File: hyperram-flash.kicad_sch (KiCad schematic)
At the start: 7 parts, among them U1 IS66WVH16M8DBLL-100B1LI

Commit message: Finish creating hierarchical buses and structure, start reconnecting signals
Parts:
- added C5: C_100n_0402, sodimm-ddr5-tester-footprints:C_0402_1005Metric, symbol sodimm-ddr5-tester:C_100n_0402
- added R10: R_100R_0402, sodimm-ddr5-tester-footprints:R_0402_1005Metric, symbol sodimm-ddr5-tester:R_100R_0402
- added R3: R_2k2_0402, sodimm-ddr5-tester-footprints:R_0402_1005Metric, symbol sodimm-ddr5-tester:R_2k2_0402
- added R4, R5: R_4k7_0402, sodimm-ddr5-tester-footprints:R_0402_1005Metric, symbol sodimm-ddr5-tester:R_4k7_0402
- added R6, R7, R8, R9: R_22R_0402, sodimm-ddr5-tester-footprints:R_0402_1005Metric, symbol sodimm-ddr5-tester:R_22R_0402
- added U3: S25FL128SAGNFI000, sodimm-ddr5-tester-footprints:WSON-8_6x8x0.5mm_P1.27mm, symbol sodimm-ddr5-tester:S25FL128SAGNFI000
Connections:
- net +3V3: now also C5.1, R3.1, R4.1, R5.1, U3.8 (V_{CC})
- net GND: now also C5.2, R10.2, U3.4 (V_{SS})
- new net: R7.1, U3.2 (SO/IO1)
- new net: R5.2, R8.1, U3.3 (~{WP}/IO2)
- new net: R4.2, R9.1, U3.7 (~{HOLD}/IO3)
- new net: R6.1, U3.5 (SI/IO0)
- new net FLASH.IO0: R6.2
- new net FLASH.IO1: R7.2
- new net FLASH.IO2: R8.2
- new net FLASH.IO3: R9.2
- new net FLASH.SCK: R10.1, U3.6 (SCK)
- new net FLASH.~{CS}: R3.2, U3.1 (~{CS})
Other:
- note added: "(Q)SPI flash"
- note added: "Master SPI Quad (x4) configuration scheme Follows Figure 2-14 7 Series FPGAs Configuration User Guide UG470 (v1.13.1)"
- moved on the sheet: C1, C2, C3, C4, R1, R2, U1

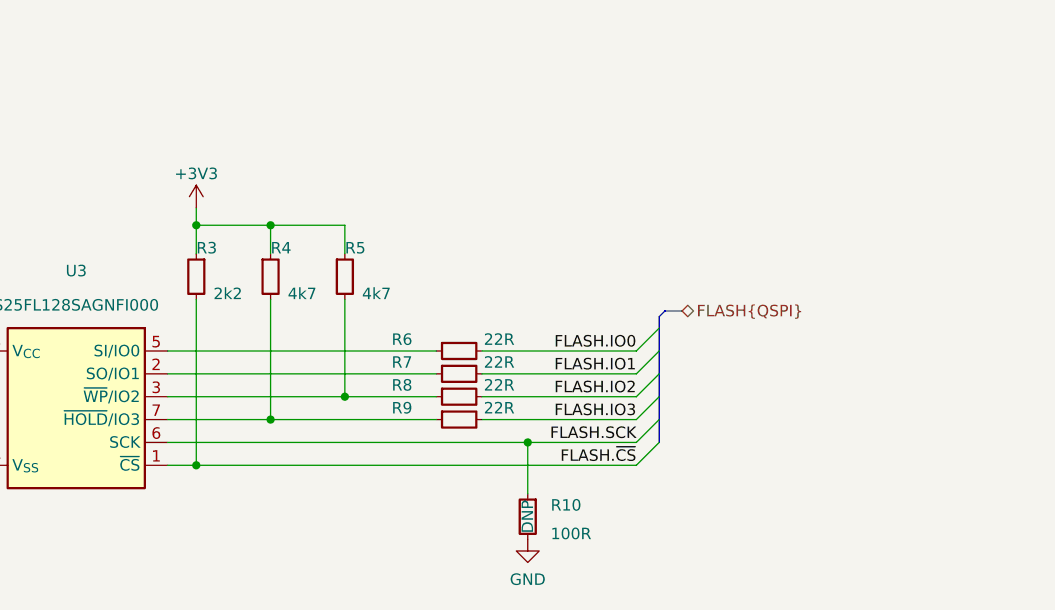
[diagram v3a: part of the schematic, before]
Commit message: Finish updating components to newest versions, improve silkscreen marking, bump revision
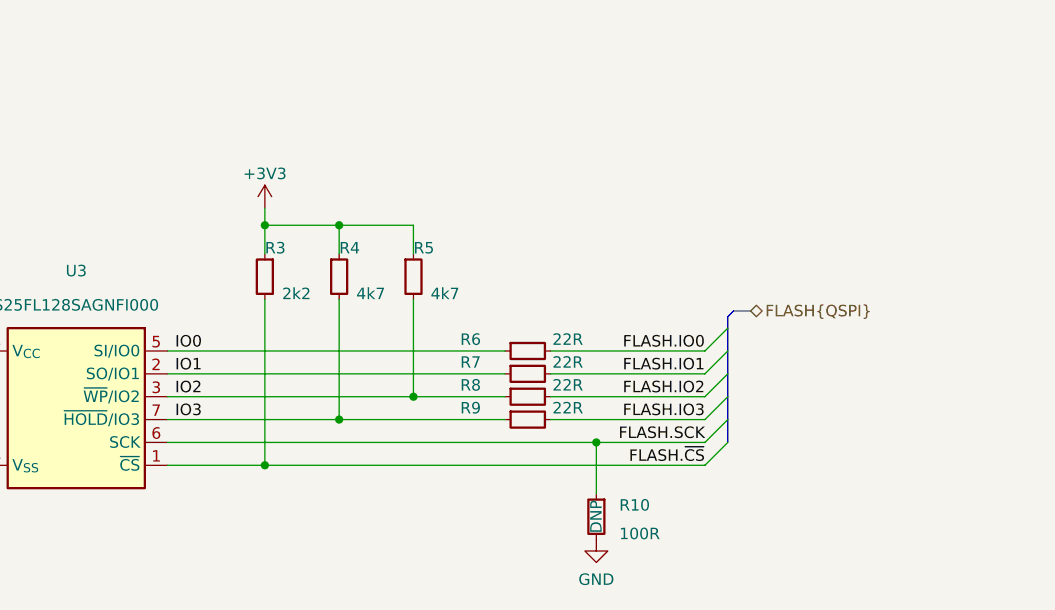
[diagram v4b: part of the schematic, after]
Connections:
- net IO1: now reaches R7.1, U3.2 (SO/IO1)
- net IO2: now reaches R5.2, R8.1, U3.3 (~{WP}/IO2)
- net IO3: now reaches R4.2, R9.1, U3.7 (~{HOLD}/IO3)
- net IO0: now reaches R6.1, U3.5 (SI/IO0)
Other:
- moved on the sheet: R10, R3, R4, R5, R6, R7, R8, R9

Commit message: Finish schematic cleanup
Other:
- moved on the sheet: C5, R10, R3, R4, R5, R6, R7, R8, R9, U3

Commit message: Clean schematic DRC
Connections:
- now unconnected: U1.A2 (NC), U1.A5 (NC), U1.B5 (NC), U1.C2 (NC), U1.C5 (NC)

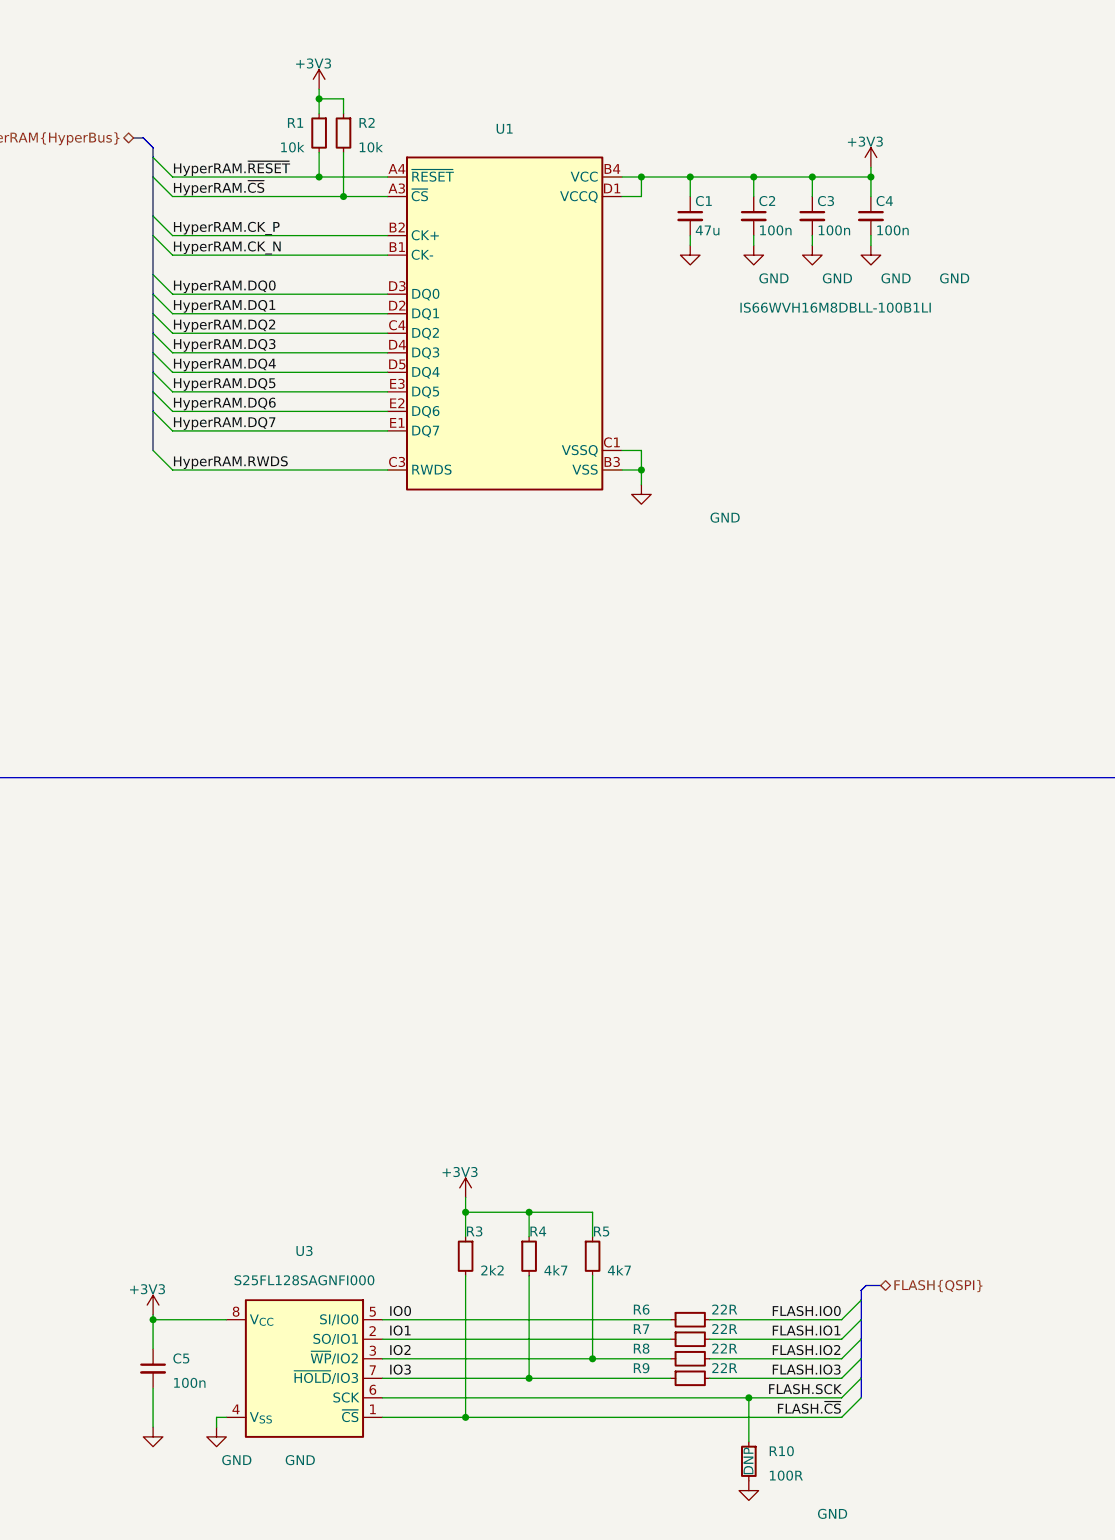
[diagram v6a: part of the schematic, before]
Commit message: Add updated components to local library
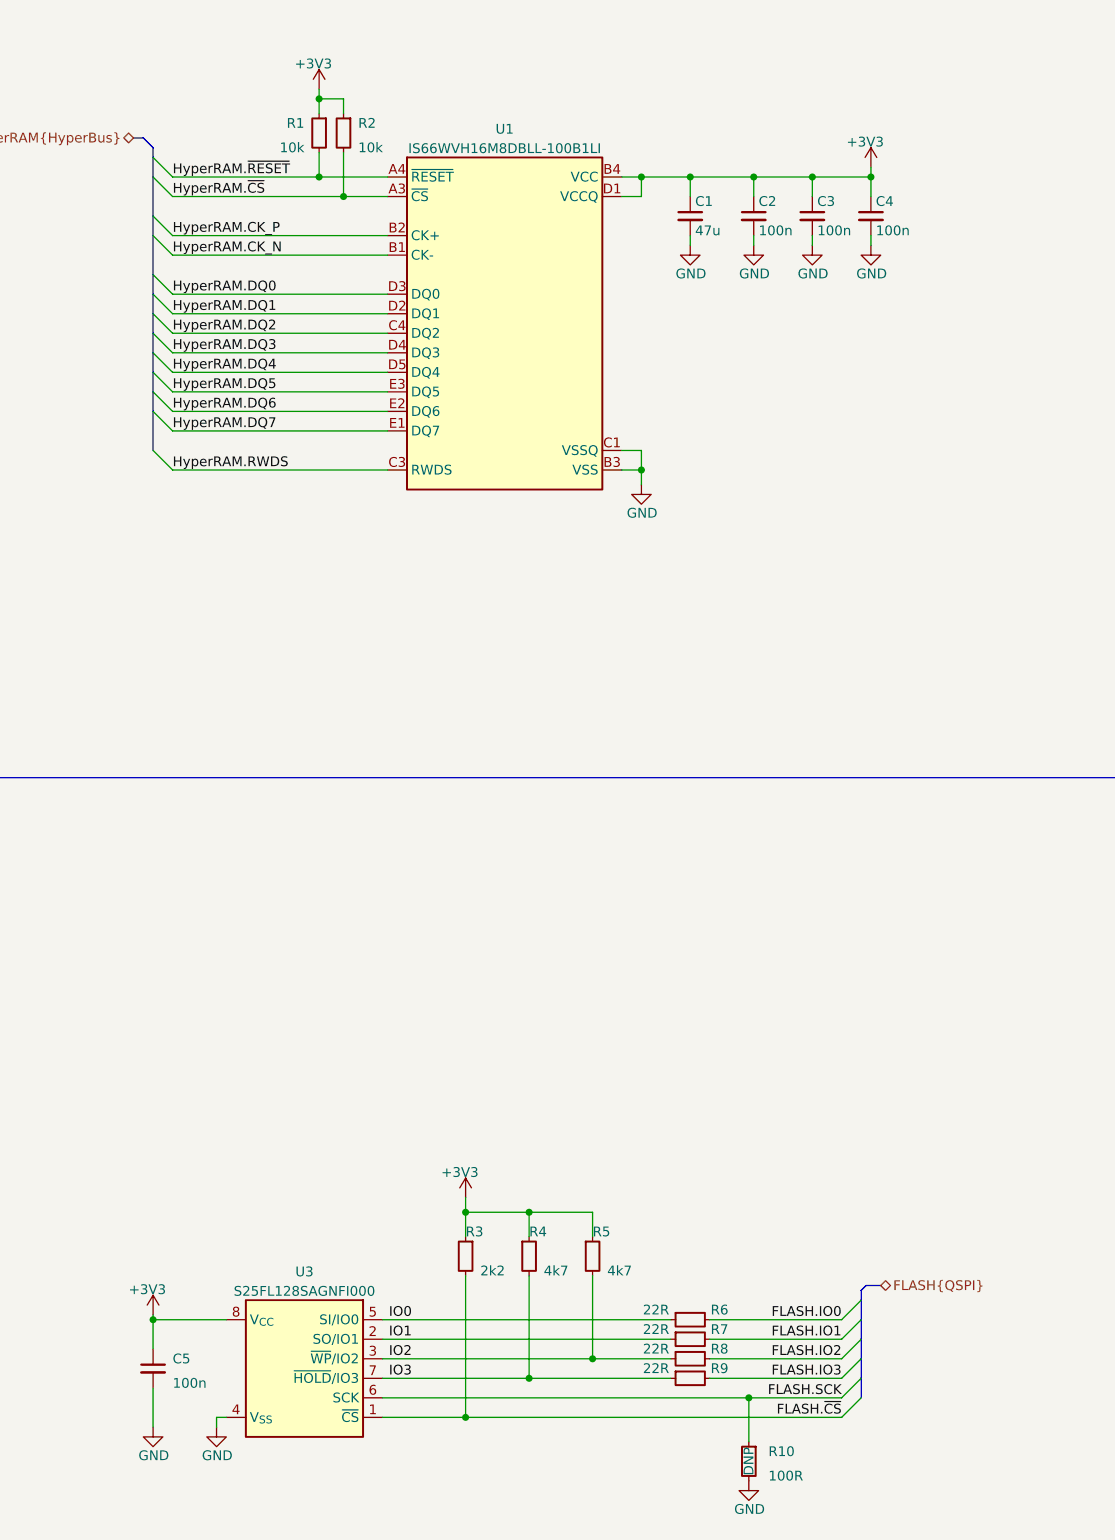
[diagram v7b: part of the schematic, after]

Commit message: [#57478] ohp release
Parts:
- C1: footprint sodimm-ddr5-tester-footprints:C_0603_1608Metric -> antmicro-footprints:C_0603_1608Metric; symbol sodimm-ddr5-tester:C_47u_0603 -> antmicroCapacitors0603:C_47u_0603
- C2, C3, C4, C5: footprint sodimm-ddr5-tester-footprints:C_0402_1005Metric -> antmicro-footprints:C_0402_1005Metric; symbol sodimm-ddr5-tester:C_100n_0402 -> antmicroCapacitors0402:C_100n_0402
- R1, R2: footprint sodimm-ddr5-tester-footprints:R_0402_1005Metric -> antmicro-footprints:R_0402_1005Metric; symbol sodimm-ddr5-tester:R_10k_0402 -> antmicroResistors0402:R_10k_0402
- R10: footprint sodimm-ddr5-tester-footprints:R_0402_1005Metric -> antmicro-footprints:R_0402_1005Metric; symbol sodimm-ddr5-tester:R_100R_0402 -> antmicroResistors0402:R_100R_0402; now not fitted; now left out of the parts list
- R3: footprint sodimm-ddr5-tester-footprints:R_0402_1005Metric -> antmicro-footprints:R_0402_1005Metric; symbol sodimm-ddr5-tester:R_2k2_0402 -> antmicroResistors0402:R_2k2_0402
- R4, R5: footprint sodimm-ddr5-tester-footprints:R_0402_1005Metric -> antmicro-footprints:R_0402_1005Metric; symbol sodimm-ddr5-tester:R_4k7_0402 -> antmicroResistors0402:R_4k7_0402
- R6, R7, R8, R9: footprint sodimm-ddr5-tester-footprints:R_0402_1005Metric -> antmicro-footprints:R_0402_1005Metric; symbol sodimm-ddr5-tester:R_22R_0402 -> antmicroResistors0402:R_22R_0402
- U1: footprint sodimm-ddr5-tester-footprints:FBGA-25-24_6x8mm_Layout5x5_P1mm -> antmicro-footprints:FBGA-25-24_6x8mm_Layout5x5_P1mm; symbol sodimm-ddr5-tester:IS66WVH16M8DBLL-100B1LI -> antmicroMemory:IS66WVH16M8DBLL-100B1LI
- U3: footprint sodimm-ddr5-tester-footprints:WSON-8_6x8x0.5mm_P1.27mm -> antmicro-footprints:WSON-8_6x8x0.5mm_P1.27mm; symbol sodimm-ddr5-tester:S25FL128SAGNFI000 -> antmicroMemory:S25FL128SAGNFI000
